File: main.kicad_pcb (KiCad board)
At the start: 2 copper layers, 321.7 x 102.8 mm, 110 parts, among them SW1 Kailh-Choc, SW10 Kailh-Choc, SW11 Kailh-Choc, SW12 Kailh-Choc, SW13 Kailh-Choc, SW14 Kailh-Choc, SW15 Kailh-Choc, SW16 Kailh-Choc, SW17 Kailh-Choc, SW18 Kailh-Choc, SW19 Kailh-Choc, SW2 Kailh-Choc, SW20 Kailh-Choc, SW21 Kailh-Choc, SW22 Kailh-Choc, SW23 Kailh-Choc, SW24 Kailh-Choc, SW25 Kailh-Choc, SW26 Kailh-Choc, SW27 Kailh-Choc, SW28 Kailh-Choc, SW29 Kailh-Choc, SW3 Kailh-Choc, SW30 Kailh-Choc, SW31 Kailh-Choc, SW32 Kailh-Choc, SW33 Kailh-Choc, SW34 Kailh-Choc, SW35 Kailh-Choc, SW36 Kailh-Choc, SW37 Kailh-Choc, SW38 Kailh-Choc, SW39 Kailh-Choc, SW4 Kailh-Choc, SW40 Kailh-Choc, SW5 Kailh-Choc, SW6 Kailh-Choc, SW7 Kailh-Choc, SW8 Kailh-Choc, SW9 Kailh-Choc, U1 nice_nano, U2 nice_nano

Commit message: Finished, time for cleanup
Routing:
- net COL2: track 171.9 -> 187.2 mm
- net Net-(D27-A): track 0.07 -> 3.18 mm
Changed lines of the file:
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@@
     (property "ki_description" "Switch, single pole double throw")
     (property "ki_keywords" "switch single-pole double-throw spdt ON-ON")
-    (attr through_hole)
+    (attr smd)
     (fp_text reference "SW_POWER1" (at 0 0.889) (layer "B.SilkS") hide
         (effects (font (size 0.6 0.6) (thickness 0.12)) (justify mirror))
@@
     (property "ki_description" "Switch, single pole double throw")
     (property "ki_keywords" "switch single-pole double-throw spdt ON-ON")
-    (attr through_hole)
+    (attr smd)
     (fp_text reference "SW_POWER0" (at 0 0.889) (layer "B.SilkS") hide
         (effects (font (size 0.6 0.6) (thickness 0.12)) (justify mirror))
@@
   (segment (start 152.136649 128.349817) (end 152.136649 131.106729) (width 0.25) (layer "B.Cu") (net 30))
   (segment (start 170.136652 143.384106) (end 170.188896 143.43635) (width 0.25) (layer "B.Cu") (net 31))
+  (segment (start 170.188896 142.402062) (end 170.136652 142.349818) (width 0.25) (layer "B.Cu") (net 31))
+  (segment (start 170.188896 145.43635) (end 170.188896 142.402062) (width 0.25) (layer "B.Cu") (net 31))
   (segment (start 98.136647 148.349318) (end 98.136647 152.791101) (width 0.25) (layer "B.Cu") (net 32))
   (segment (start 98.136647 152.791101) (end 98.433896 153.08835) (width 0.25) (layer "B.Cu") (net 32))
@@
   (segment (start 253.226875 158.577383) (end 253.799313 159.149821) (width 0.25) (layer "B.Cu") (net 41))
   (segment (start 328.454873 141.523821) (end 328.427357 141.551337) (width 0.25) (layer "B.Cu") (net 41))
-  (segment (start 246.543762 149.431267) (end 249.537632 149.431267) (width 0.25) (layer "B.Cu") (net 41))
+  (segment (start 242.399718 144.587752) (end 242.399718 153.575707) (width 0.25) (layer "B.Cu") (net 41))
   (segment (start 283.226876 146.136829) (end 283.226876 144.11165) (width 0.25) (layer "B.Cu") (net 41))
   (segment (start 280.305278 147.01523) (end 280.53987 147.249823) (width 0.25) (layer "B.Cu") (net 41))
   (segment (start 290.862873 137.185318) (end 290.826875 137.14932) (width 0.25) (layer "B.Cu") (net 41))
+  (segment (start 244.537712 142.449758) (end 242.399718 144.587752) (width 0.25) (layer "B.Cu") (net 41))
   (segment (start 328.427357 141.551337) (end 328.427357 150.147803) (width 0.25) (layer "B.Cu") (net 41))
   (segment (start 280.53987 147.249823) (end 282.113882 147.249823) (width 0.25) (layer "B.Cu") (net 41))
-  (segment (start 236.824875 159.150154) (end 246.543762 149.431267) (width 0.25) (layer "B.Cu") (net 41))
   (segment (start 275.526975 147.015231) (end 280.305278 147.01523) (width 0.25) (layer "B.Cu") (net 41))
   (segment (start 253.226875 153.12051) (end 253.226875 158.577383) (width 0.25) (layer "B.Cu") (net 41))
+  (segment (start 249.762891 142.449758) (end 244.537712 142.449758) (width 0.25) (layer "B.Cu") (net 41))
+  (segment (start 242.399718 153.575707) (end 236.824875 159.15055) (width 0.25) (layer "B.Cu") (net 41))
   (segment (start 290.826875 120.149319) (end 290.826875 137.14932) (width 0.25) (layer "B.Cu") (net 41))
+  (segment (start 251.551873 144.23874) (end 249.762891 142.449758) (width 0.25) (layer "B.Cu") (net 41))
+  (segment (start 253.226875 153.12051) (end 251.551873 151.445508) (width 0.25) (layer "B.Cu") (net 41))
   (segment (start 328.427357 150.147803) (end 328.454873 150.175319) (width 0.25) (layer "B.Cu") (net 41))
   (segment (start 272.117383 150.424823) (end 275.526975 147.015231) (width 0.25) (layer "B.Cu") (net 41))
-  (segment (start 249.537632 149.431267) (end 253.226875 153.12051) (width 0.25) (layer "B.Cu") (net 41))
+  (segment (start 251.551873 151.445508) (end 251.551873 144.23874) (width 0.25) (layer "B.Cu") (net 41))
   (segment (start 335.820873 154.366319) (end 327.565873 154.366319) (width 0.25) (layer "F.Cu") (net 42))
   (segment (start 336.994206 153.192986) (end 335.820873 154.366319) (width 0.25) (layer "F.Cu") (net 42))

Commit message: Flipped right board
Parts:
- Bat+1, BatGND1, D18, D19, D20, D21, D22, D23, D24, D25, D26, D27, D28, D29, D30, D31, D32, D33, D34, D35, D36, D37, Display2, REF_PUCK_R, RSW1, SW18, SW19, SW20, SW21, SW22, SW23, SW24, SW25, SW26, SW27, SW28, SW29, SW30, SW31, SW32, SW33, SW34, SW35, SW36, SW37, kibuzzard-63658823, kibuzzard-63658865, kibuzzard-636588C8, kibuzzard-636592CC, kibuzzard-63659465: moved to B.Cu
- SW_POWER1, U2, kibuzzard-6361375E, kibuzzard-63659328, kibuzzard-6365950B, kibuzzard-63703FC3: moved to F.Cu
- moved D13 164.2 mm to (139.5, 160.0)
- moved D14 164.2 mm to (157.6, 167.5)
- moved D16 164.2 mm to (167.0, 188.8)
- moved D39 164.2 mm to (187.1, 199.0)
- moved SW12 164.2 mm to (112.9, 165.2)
- moved SW15 164.2 mm to (166.9, 168.2)
- moved SW17 164.2 mm to (177.4, 193.5)
- moved SW39 164.2 mm to (193.6, 205.0)
- moved SW7 164.2 mm to (112.9, 148.2)
- moved kibuzzard-63659477 164.2 mm to (189.2, 186.7)
- moved Bat+0 164.2 mm to (177.9, 141.1)
- moved BatGND0 164.2 mm to (193.5, 141.1)
- moved D1 164.2 mm to (103.6, 146.1)
- moved D10 164.2 mm to (172.2, 159.6)
- moved D11 164.2 mm to (103.6, 180.6)
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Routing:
- added copper zone on B.Cu, net GND
- added copper zone on F.Cu, net GND
- removed copper zone on B.Cu, net (none)
- removed copper zone on F.Cu, net (none)
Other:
- board size 321.7 x 102.8 mm -> 271.6 x 124.6 mm

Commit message: Flipped right side and added mouse bites
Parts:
- added mouse-bite-2mm-slot: VAL**, urchin-footprints:mouse-bite-5mm-slot-with-space-for-track, F.Cu at (213.2, 139.9)
- added mouse-bite-2mm-slot: VAL**, urchin-footprints:mouse-bite-5mm-slot-with-space-for-track, F.Cu at (213.2, 163.9)
- moved D16 17.8 mm to (183.9, 183.2)
- moved D40 17.8 mm to (102.4, 176.7)
- moved D9 17.8 mm to (174.4, 151.7)
- moved SW10 17.8 mm to (183.8, 145.5)
- moved SW_POWER0 17.8 mm to (202.7, 135.7)
- moved kibuzzard-6361375E 17.8 mm to (174.4, 185.0)
- moved kibuzzard-636588C8 17.8 mm to (204.3, 152.1)
- moved SW2 17.8 mm to (129.8, 125.5)
- moved SW3 17.8 mm to (147.8, 119.5)
- moved SW4 17.8 mm to (165.8, 126.0)
- moved Bat+0 17.8 mm to (194.8, 135.4)
- moved BatGND0 17.8 mm to (210.3, 135.5)
- moved D1 17.8 mm to (120.4, 140.4)
- moved D10 17.8 mm to (189.0, 153.9)
- moved D11 17.8 mm to (120.4, 175.0)
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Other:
- board size 271.6 x 124.6 mm -> 268.1 x 124.6 mm

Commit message: Moved right front to right side
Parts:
- Bat+0, BatGND0, D1, D10, D11, D12, D13, D14, D15, D16, D17, D2, D3, D38, D39, D4, D40, D5, D6, D7, D8, D9, Display1, REF_PUCK_R, RSW0, SW1, SW10, SW11, SW12, SW13, SW14, SW15, SW16, SW17, SW2, SW3, SW38, SW39, SW4, SW40, SW5, SW6, SW7, SW8, SW9, SW_POWER1, U2, kibuzzard-6361375E, kibuzzard-63658830, kibuzzard-6365884B, kibuzzard-636588C8, kibuzzard-63659296, kibuzzard-63659328, kibuzzard-63659477, kibuzzard-6365950B, kibuzzard-63703FC3, mouse-bite-2mm-slot (x2): moved to B.Cu
- Bat+1, BatGND1, D18, D19, D20, D21, D22, D23, D24, D25, D26, D27, D28, D29, D30, D31, D32, D33, D34, D35, D36, D37, Display2, REF_PUCK_R, RSW1, SW18, SW19, SW20, SW21, SW22, SW23, SW24, SW25, SW26, SW27, SW28, SW29, SW30, SW31, SW32, SW33, SW34, SW35, SW36, SW37, SW_POWER0, U1, kibuzzard-6361375E, kibuzzard-63658823, kibuzzard-63658865, kibuzzard-636588C8, kibuzzard-636592CC, kibuzzard-63659465, kibuzzard-6365951E: moved to F.Cu
- moved SW35 99.2 mm to (218.1, 201.5), turned to 40 degrees
- moved SW39 94.9 mm to (212.7, 104.5), turned to 40 degrees
- moved D35 89.5 mm to (225.3, 196.7), turned to 130 degrees
- moved D39 82.8 mm to (206.1, 110.5), turned to 130 degrees
- moved SW33 76.3 mm to (234.4, 190.0), turned to 30 degrees
- moved SW17 72.0 mm to (196.4, 116.0), turned to 30 degrees
- moved kibuzzard-6361375E 70.2 mm to (254.2, 187.0), turned to -165 degrees
- moved D33 69.5 mm to (242.7, 186.7), turned to 120 degrees
- moved D34 67.7 mm to (244.9, 185.8), turned to 105 degrees
- moved kibuzzard-63658823 67.7 mm to (254.1, 185.8), turned to 15 degrees
- moved kibuzzard-6361375E 66.1 mm to (176.6, 118.9), turned to -165 degrees
- moved SW3 64.9 mm to (150.0, 184.3)
- moved D17 64.8 mm to (188.5, 119.6), turned to -60 degrees
- moved kibuzzard-63658830 63.3 mm to (177.0, 120.3), turned to 15 degrees
- moved RSW1 62.8 mm to (217.6, 183.3), turned to 74 degrees
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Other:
- outline, holes or cut-outs redrawn

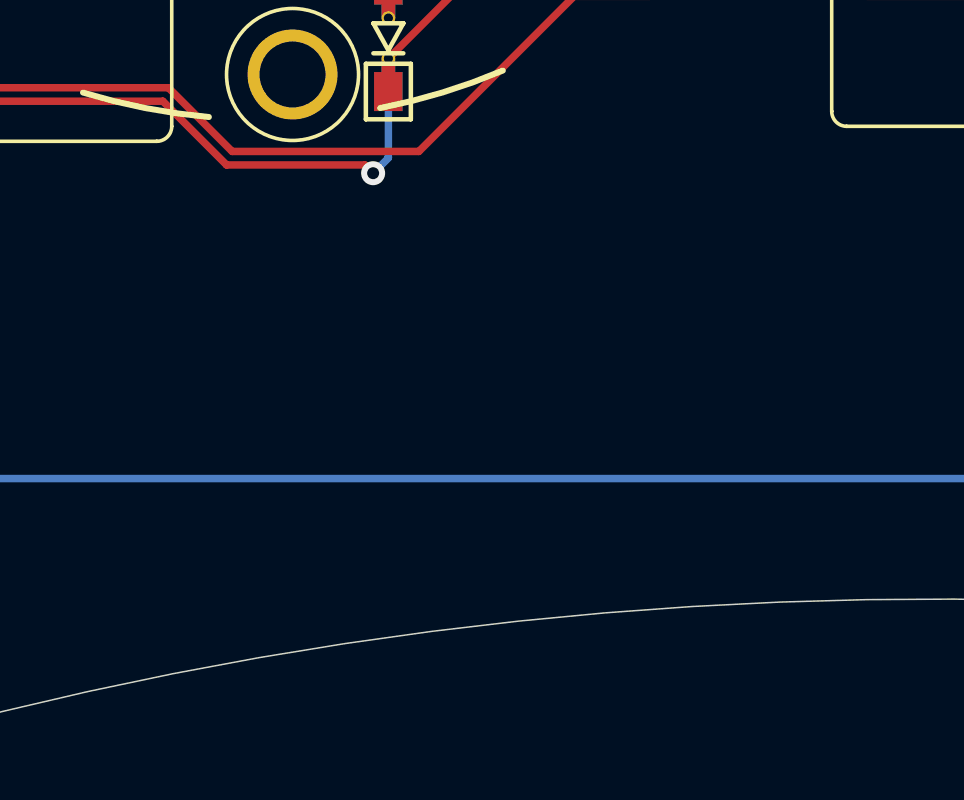
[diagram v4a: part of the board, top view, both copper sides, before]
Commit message: Added brain icon
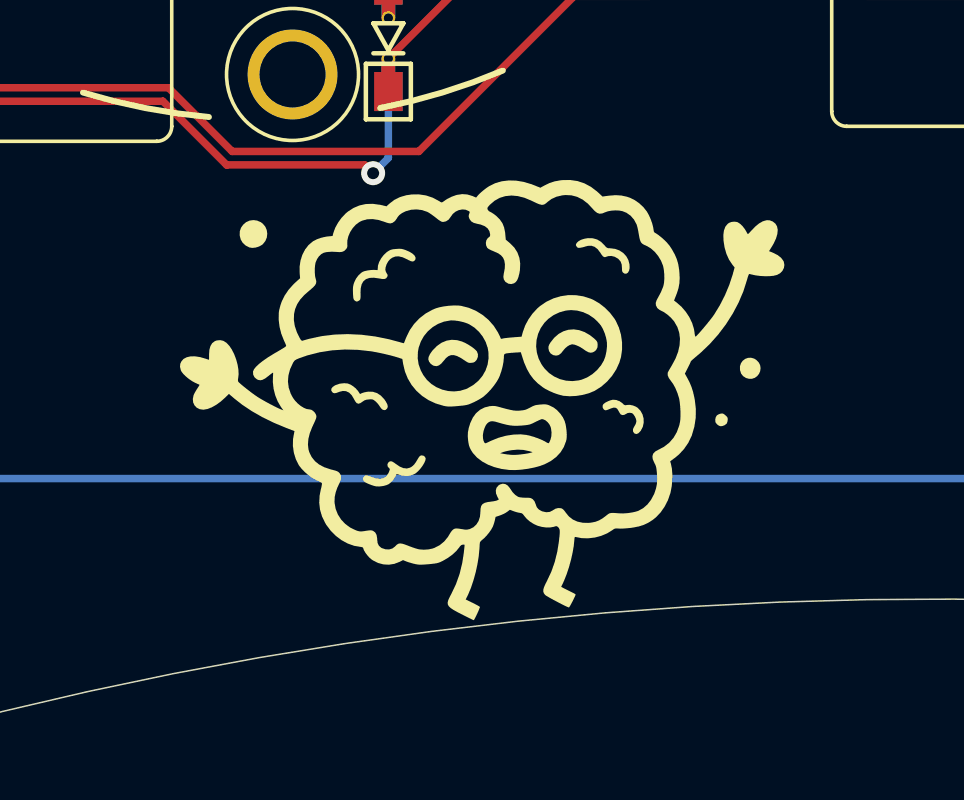
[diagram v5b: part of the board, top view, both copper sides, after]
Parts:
- added G***: LOGO, LOGO, F.Cu at (280.4, 177.8)

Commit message: Changed icon to copper
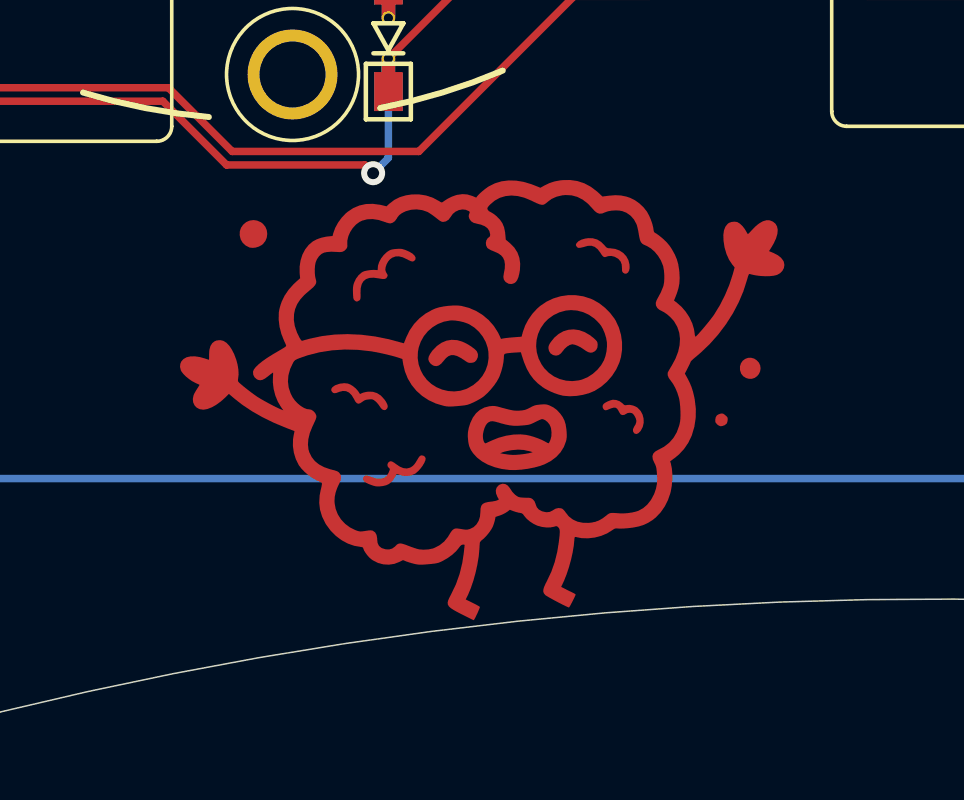
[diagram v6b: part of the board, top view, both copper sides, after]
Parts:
- removed the G*** at (280.4, 177.8)
- added G***: brain_copper, urchin-footprints:brain_copper, F.Cu at (280.4, 177.8)

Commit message: Added pads for niceview cover
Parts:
- added ?: , , F.Cu at (230.6, 176.2)
- added ?: , , F.Cu at (208.1, 117.1)
- added ?: , , F.Cu at (193.6, 125.6)
- added ?: , , F.Cu at (216.1, 184.7)
- moved D37 264.1 mm to (84.8, 125.2), turned to -90 degrees
- moved D36 259.4 mm to (84.8, 142.1), turned to -90 degrees
- moved SW37 246.8 mm to (93.4, 126.2), turned to 180 degrees
- moved SW36 242.0 mm to (93.4, 143.2), turned to 180 degrees
- moved SW40 241.0 mm to (332.3, 175.5), turned to 180 degrees
- moved SW38 236.7 mm to (332.3, 158.5), turned to 180 degrees
- moved D32 228.0 mm to (102.9, 127.1), turned to -90 degrees
- moved D40 224.6 mm to (323.6, 176.7), turned to 90 degrees
- moved D22 223.3 mm to (102.9, 161.7), turned to -90 degrees
- moved D27 223.0 mm to (102.9, 144.1), turned to -90 degrees
- moved D38 219.6 mm to (323.6, 159.6), turned to 90 degrees
- moved SW32 210.8 mm to (111.4, 128.2), turned to 180 degrees
- moved SW22 206.4 mm to (111.4, 162.2), turned to 180 degrees
- moved SW27 205.8 mm to (111.4, 145.2), turned to 180 degrees
- moved SW11 204.9 mm to (314.3, 173.5), turned to 180 degrees
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- renumbered RSW1 to RSWe
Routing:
- net R_COL0: track 75.2 -> 82.0 mm
- net R_ROW3: track 184.6 -> 188.7 mm
- net RESET: track 50.3 -> 46.9 mm
- net COL1: track 165.6 -> 163.1 mm
- net ROW3: track 175.7 -> 177.9 mm
- net COL4: track 81.1 -> 82.8 mm
- net R_RESET: track 37.4 -> 35.8 mm
- net R_GND: track 77.0 -> 76.3 mm
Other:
- outline, holes or cut-outs redrawn
